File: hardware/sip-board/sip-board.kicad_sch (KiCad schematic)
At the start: 92 parts, among them IC1 XC7S15-1CPGA196C, IC2 MT25QL512ABB1EW9-0SIT, J1 Conn_02x03_Odd_Even, J2 Conn_01x10_Pin, J3 Conn_01x10_Pin, J4 Conn_01x10_Pin, J5 Conn_01x10_Pin, U1 TLV75718PDRV, U2 TLV75733PDRV, U3 TLV75710PDRV

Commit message: placement done, new dip switch
need to start picking parts and routing
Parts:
- removed C1, C38: 10u, Capacitor_SMD:C_0402_1005Metric, symbol Device:C_Small
- removed C10, C12, C13, C20, C21, C22, C23, C28, C30, C31, C32, C33, C34, C7, C8, C9: 0.47u, Capacitor_SMD:C_0201_0603Metric, symbol Device:C_Small
- removed C11: 10u, Capacitor_SMD:C_0201_0603Metric, symbol Device:C_Small
- removed C14, C15, C25, C5: 100u, Capacitor_SMD:C_0402_1005Metric, symbol Device:C_Small
- removed C16, C17, C18, C19, C26, C27, C29, C36, C37: 4.7u, Capacitor_SMD:C_0201_0603Metric, symbol Device:C_Small
- removed C2, C3: 50u, Capacitor_SMD:C_0402_1005Metric, symbol Device:C_Small
- removed C24: 47u, Capacitor_SMD:C_0201_0603Metric, symbol Device:C_Small
- removed C35: 100u, Capacitor_SMD:C_0201_0603Metric, symbol Device:C_Small
- removed C4, C6: 1u, Capacitor_SMD:C_0201_0603Metric, symbol Device:C_Small
- removed CFG1: SW_DIP_x03, Button_Switch_SMD:SW_DIP_SPSTx03_Slide_6.7x9.18mm_W6.73mm_P2.54mm_LowProfile_JPin, symbol Switch:SW_DIP_x03
- removed D4, D5: LED, LED_SMD:LED_0201_0603Metric, symbol Device:LED
- removed IC1: XC7S15-1CPGA196C, fpga_stuff:BGA196C50P14X14_800X800X110, symbol XC7S15-1CPGA196C:XC7S15-1CPGA196C
- removed IC2: MT25QL512ABB1EW9-0SIT, hardware:MT25QL512ABB1EW9-0SIT, symbol MT25QL512ABB1EW9-0SIT:MT25QL512ABB1EW9-0SIT
- removed J1: Conn_02x03_Odd_Even, hardware:TAG_TC2030-IDC-NL, symbol Connector_Generic:Conn_02x03_Odd_Even
- removed J2, J3, J4, J5: Conn_01x10_Pin, Connector_PinHeader_2.54mm:PinHeader_1x10_P2.54mm_Vertical, symbol Connector:Conn_01x10_Pin
- removed R10, R11, R12, R13, R4, R5, R6, R7, R8, R9: 10k, Resistor_SMD:R_0201_0603Metric, symbol Device:R_Small
- removed R14, R15, R16, R17, R21: 4k7, Resistor_SMD:R_0201_0603Metric, symbol Device:R_Small
- removed R18: 2k3, Resistor_SMD:R_0201_0603Metric, symbol Device:R_Small
- removed R19: 3k, Resistor_SMD:R_0201_0603Metric, symbol Device:R_Small
- removed R20: 5k7, Resistor_SMD:R_0201_0603Metric, symbol Device:R_Small
- removed S1: EVQ-P2R02W, hardware:EVQP2R02W, symbol EVQ-P2R02W:EVQ-P2R02W
- removed U1: TLV75718PDRV, Package_SON:WSON-6-1EP_2x2mm_P0.65mm_EP1x1.6mm, symbol Regulator_Linear:TLV75718PDRV
- removed U10, U11, U12, U13, U14, U5, U6, U7, U8, U9: ~, hardware:NXB0104GU12X, symbol custom_symbols:NXB0104_XQFN12
- removed U2: TLV75733PDRV, Package_SON:WSON-6-1EP_2x2mm_P0.65mm_EP1x1.6mm, symbol Regulator_Linear:TLV75733PDRV
- removed U3: TLV75710PDRV, Package_SON:WSON-6-1EP_2x2mm_P0.65mm_EP1x1.6mm, symbol Regulator_Linear:TLV75710PDRV
- added D1, D2: LED, LED_SMD:LED_0402_1005Metric, symbol Device:LED
- D3, DONE1: footprint LED_SMD:LED_0201_0603Metric -> LED_SMD:LED_0402_1005Metric
- R1, R2, R3: value 1k -> R_Small
- renumbered TP2 to TP1, TP3 to TP2, TP4 to TP3, TP5 to TP4, TP6 to TP5, TP7 to TP6, TP1 to TP7
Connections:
- net M0_CONFIG is gone; now on net +3V3: R1.1
- net M1_CONFIG is gone; now on net +1V8: R2.1
- net M2_CONFIG is gone; now on net +1V0: R3.1
- net GND: now also D1.1 (K), D2.1 (K); no longer R1.2, R2.2, R3.2
- net at D3.2 (A): now also R3.2
- new net: D1.2 (A), R1.2
- new net: D2.2 (A), R2.2
- no-connect marks 18 -> 0
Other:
- added sheet Config + Programming (peripherals.kicad_sch)
- added sheet Decaps (decap.kicad_sch)
- added sheet FPGA (fpga.kicad_sch)
- added sheet Pinout (pinout_external.kicad_sch)
- added sheet Voltage Regulators - 3V3, 1V8, 1V0 (pd.kicad_sch)
- note added: "Board -> Outside World"
- note added: "Config + Programming"
- note added: "Decaps"
- note added: "FPGA"
- note added: "LDOs"
- note added: "Power Indicators"
- note added: "To look at subsheets, double click the above boxes or use the left "Schematic Hierarchy" pane to click on them."
- note removed: "3V3<->5V level shifters (FPGA <-> Z80 System)"
- note removed: "5V -> 1.0V VCCINT LDO: 2x2 mm"
- note removed: "5V -> 1.8V VCCAUX LDO: 2x2 mm"
- note removed: "5V -> 3.3V VCCO LDO: 2x2 mm"
- note removed: "5V -> X.X LDOs WSON-6 package"
- note removed: "Boot Configuration"
- note removed: "Configuration Banks Voltage Select section in the config user guide; tldr we are running of 3v3 for SPI flash so CFGBVS needs to be 3v3 as well"
- note removed: "Decoupling Capacitors"
- note removed: "Going with MT25QL512 ... directly supported by Vivado"
- note removed: "JTAG Connector"
- note removed: "M[2:0] = 001 for Master SPI config"
- note removed: "Per datasheet, W# must be pulled high initially to enable writes, regardless of current mode"
- note removed: "Pins 1-20 (ascending order)"
- note removed: "Pins 21-40 (ascending order)"
- note removed: "Reset Logic"
- note removed: "SPI Memory"
- note removed: "The recommended power-on sequence is VCCINT, VCCBRAM, VCCAUX, and VCCO to achieve minimum current draw and ensure that the I/Os are 3-stated at power-on. The recommended power-off sequence is the reverse of the power-on sequence. If VCCINT and VCCBRAM have the same recommended voltage levels then both can be powered by the same supply and ramped simultaneously. If VCCAUX and VCCO have the same re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"
- note removed: "This A3 --> is VCC (5V) on original Z80"
- note removed: "This A4 pin --> is GND on original Z80"
- note removed: "UG470 7-Series pg.25"
- note removed: "UG470 pg 22"
- note removed: "UG470 pg27 Need pull-ups on DQ2/3, CS"
- note removed: "We aren't daisy chaining any JTAG pins, so we don't need pull-ups, per UG470"
- note removed: "We want pullup on OE"
- note removed: "Xilinx recommends specific power on sequence for each LDO, but I haven't found small enough LDOs with enable pins, so we're scaling up the capacitor values for now. Fix!"
- note removed: "Z80 System Connectors PIN HEADERS!"
- note removed: "`CLK` signal is routed into H4 (MRCC) as it can be used in global clock tree this must be configured in the constraints file"
- note removed: "https://docs.amd.com/r/en-US/xapp586-spi-flash/SPI-Flash-Configuration-Interface https://docs.amd.com/r/2021.2-English/ug908-vivado-programming-debugging/Spartan-7-Configuration-Memory-Devices"
- note removed: "https://docs.amd.com/v/u/en-US/ug483_7Series_PCB Page 14"
- note removed: "https://www.tag-connect.com/wp-content/uploads/bsk-pdf-manager/2019/12/TC2030-IDC-NL-Datasheet-Rev-B.pdf"
- company: (none) -> University of Texas at Austin / Phoenix Semiconductor
- title: (none) -> Z80 Drop In SiP Board
- moved on the sheet: DONE1, TP1, TP2, TP3, TP4, TP5, TP6, TP7

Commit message: raahhhhh my eyeballs hurt
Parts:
- added Q3, Q4, Q5: BS170F, Package_TO_SOT_SMD:SOT-23, symbol Transistor_FET:BS170F
- added R34, R36: UNKNOWN, Resistor_SMD:R_0201_0603Metric, symbol Device:R_Small
- added R35: 100k, Resistor_SMD:R_0201_0603Metric, symbol Device:R_Small
- added TP10, TP11, TP8, TP9: TestPoint, TestPoint:TestPoint_Pad_1.0x1.0mm, symbol Connector:TestPoint
- R1, R3: value R_Small -> 100k
- R2: value R_Small -> UNKNOWN
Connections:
- net +1V0: now also D1.2 (A), R1.1, TP10.1; no longer R3.1
- net +1V8: now also D2.2 (A), R3.1, TP9.1; no longer R2.1
- net +3V3: now also D3.2 (A), R35.1, TP8.1; no longer R1.1
- net GND: now also Q3.2 (S), Q4.2 (S), Q5.2 (S), TP11.1; no longer D1.1 (K), D2.1 (K), D3.1 (K)
- net PGOOD: now reaches R1.2
- net PGOOD: now also R3.2, Q3.1 (G), Q4.1 (G), Q5.1 (G), R35.2; no longer D1.2 (A)
- net at R2.2: now also Q3.3 (D); no longer D2.2 (A)
- new net: D3.1 (K), R36.1
- new net: Q5.3 (D), R36.2
- new net: D1.1 (K), R2.1
- new net: Q4.3 (D), R34.2
- new net: D2.1 (K), R34.1
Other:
- note added: "Power"
- note removed: "LDOs"
- moved on the sheet: TP1, TP2, TP3, TP4, TP5, TP6

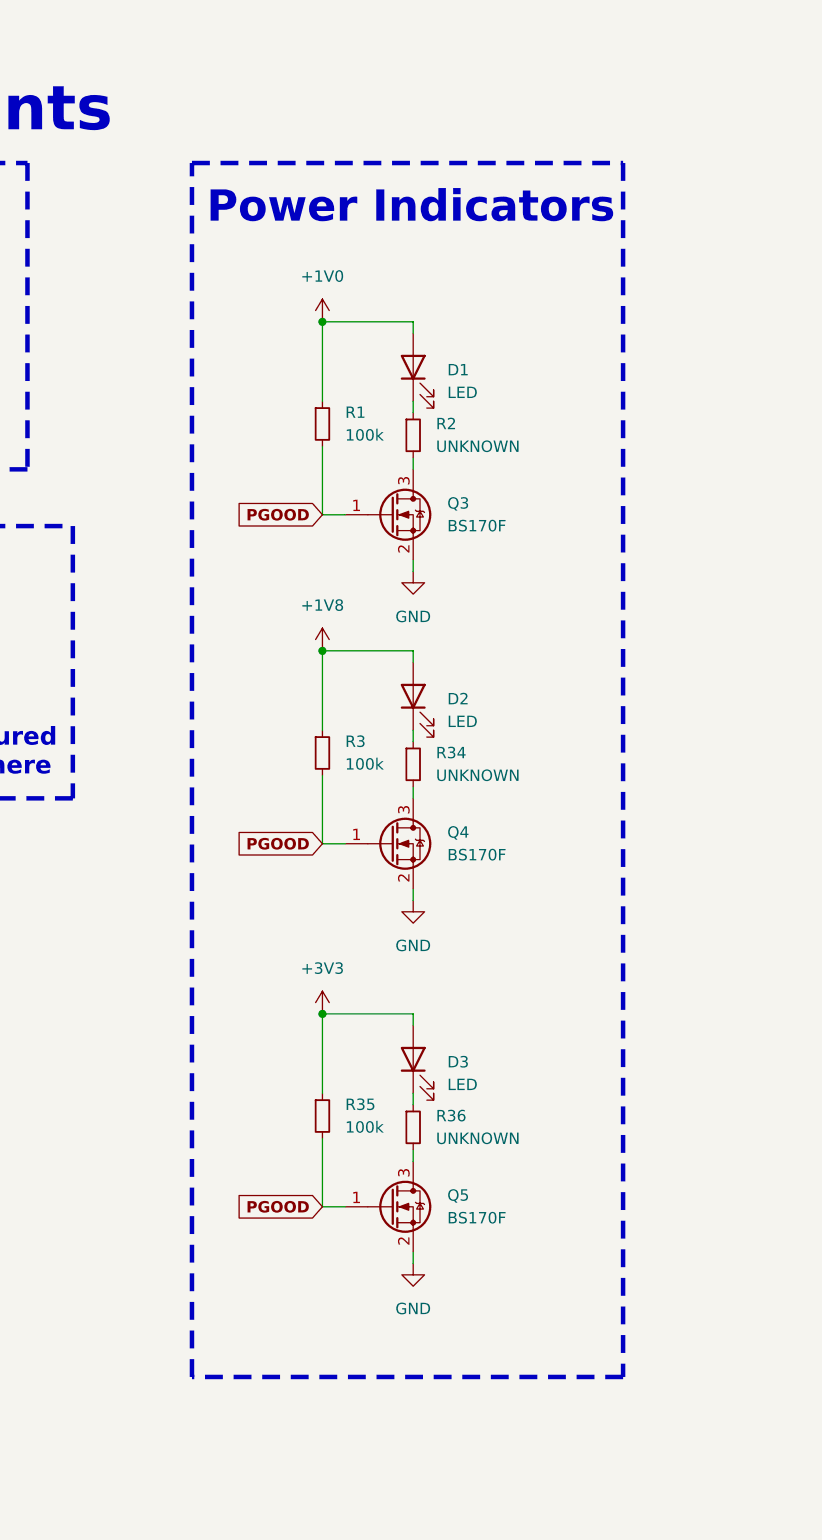
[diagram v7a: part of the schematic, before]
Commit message: remove all but 3v3 LED
not enough voltage/current from the other 2 power rails to light up an LED
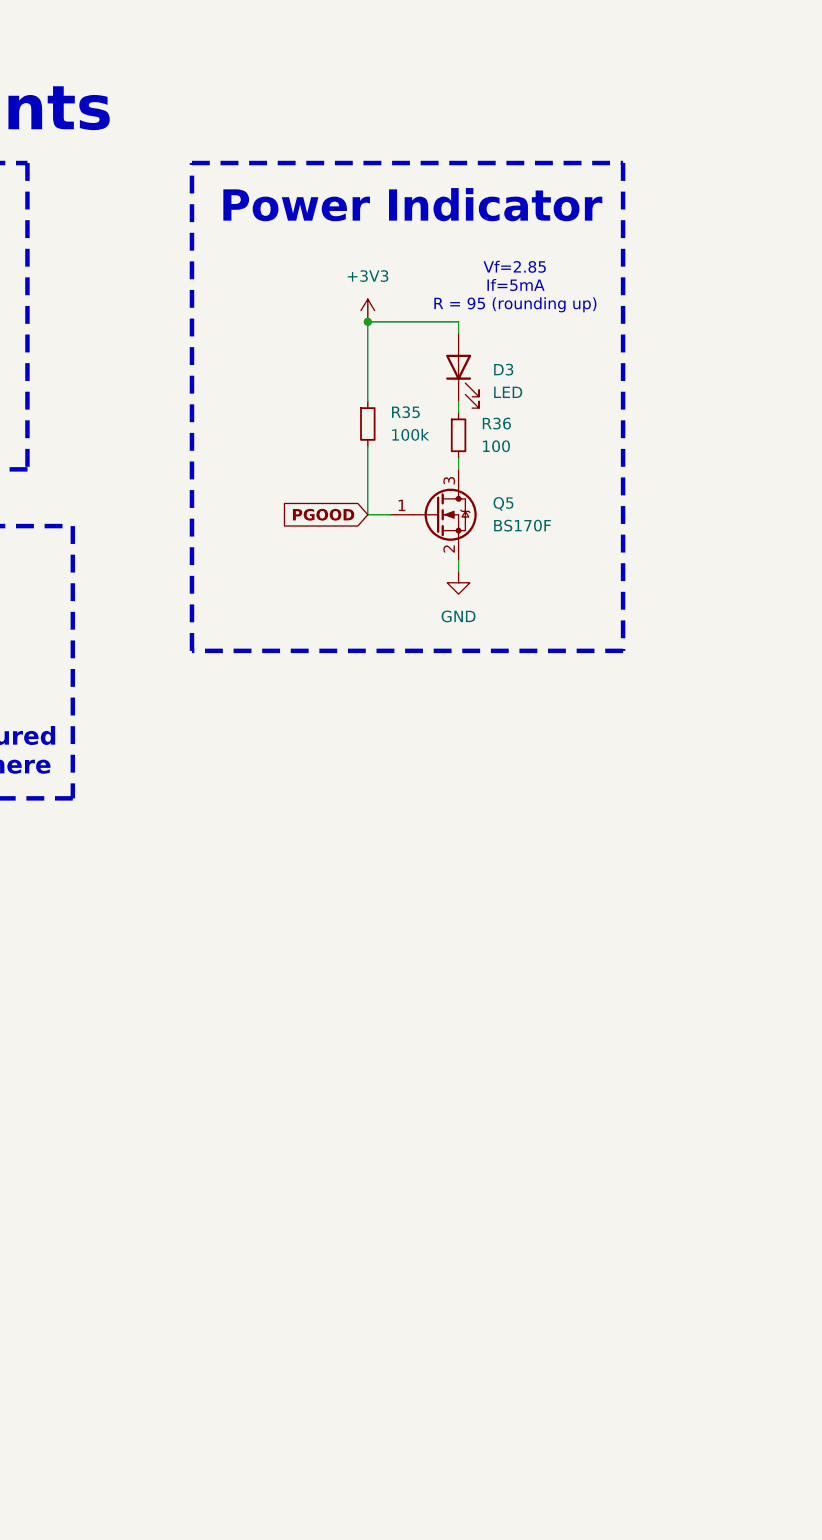
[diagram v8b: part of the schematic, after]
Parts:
- removed D1, D2: LED, LED_SMD:LED_0402_1005Metric, symbol Device:LED
- removed Q3, Q4: BS170F, Package_TO_SOT_SMD:SOT-23, symbol Transistor_FET:BS170F
- removed R1, R3: 100k, Resistor_SMD:R_0201_0603Metric, symbol Device:R_Small
- removed R2, R34: UNKNOWN, Resistor_SMD:R_0201_0603Metric, symbol Device:R_Small
- R36: value UNKNOWN -> 100
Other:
- note added: "Power Indicator"
- note added: "Vf=2.85 If=5mA R = 95 (rounding up)"
- note removed: "Power Indicators"
- moved on the sheet: D3, Q5, R35, R36
